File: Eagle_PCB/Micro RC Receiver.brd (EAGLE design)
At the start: 33 x 21.6 mm, 22 parts, among them IC2 TB6612FNG, Q1 CSTCC8M00G53-R0, U1 MIC5205-3.3, U2 ATMEGA328P_TQFP

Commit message: V 1.3
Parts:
- added C3: 10uF, SparkFun-Capacitors:EIA3216
- added R2: 20k, rcl:R0805
- added R3: 10k, rcl:R0805
- moved C6 4.13 mm to (14.3, 15.1), turned to 180 degrees
- moved R1 3.33 mm to (14.3, 13.0)
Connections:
- net A7: now also R2.1, R3.2
- net D3: now also IC2.15; no longer IC2.17
- net D5: now also IC2.17; no longer IC2.15
- net GND: now also C3.C, R3.1
- net VBAT: now also C3.A, R2.2
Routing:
- net A3: track 50.8 -> 23.0 mm
- net RESET: track 26.3 -> 19.2 mm
- net A7: track 0.00 -> 5.68 mm
- net VBAT: track 0.00 -> 4.41 mm
- net A2: track 29.6 -> 25.7 mm
- net VCC: track 38.3 -> 34.5 mm
- net A0: track 51.3 -> 47.6 mm
- net D5: track 22.1 -> 25.4 mm
- net A1: track 26.4 -> 29.4 mm
- net GND: track 58.7 -> 60.3 mm, vias 10 -> 13
- net D3: track 17.9 -> 19.2 mm
- net D9: track 17.3 -> 18.1 mm
- net RXI: track 37.1 -> 36.4 mm
- net TXO: track 34.0 -> 33.4 mm
- net D6: track 21.8 -> 22.3 mm
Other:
- board text added: "Micro RC Receiver V1.3"
- board text removed: "Micro RC Receiver V1.1"

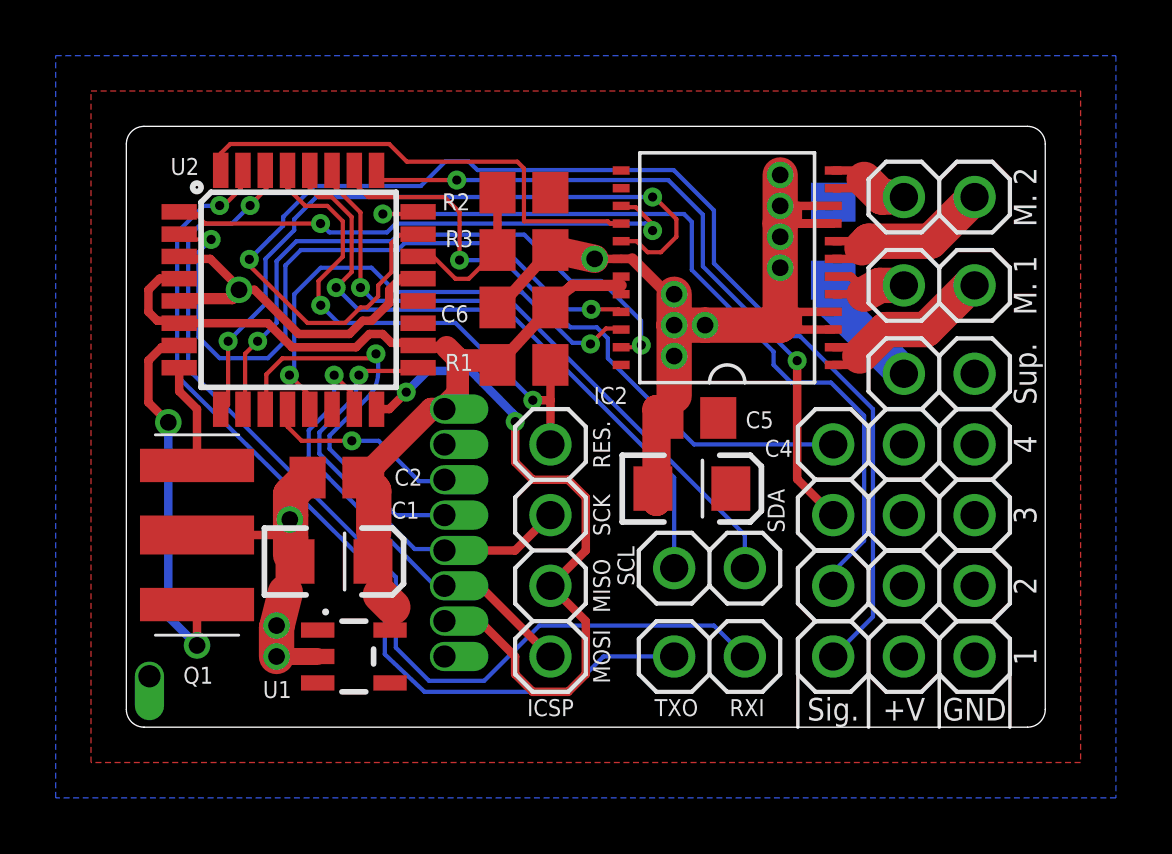
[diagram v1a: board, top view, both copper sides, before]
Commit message: V1.4
GND plane and decoupling improved
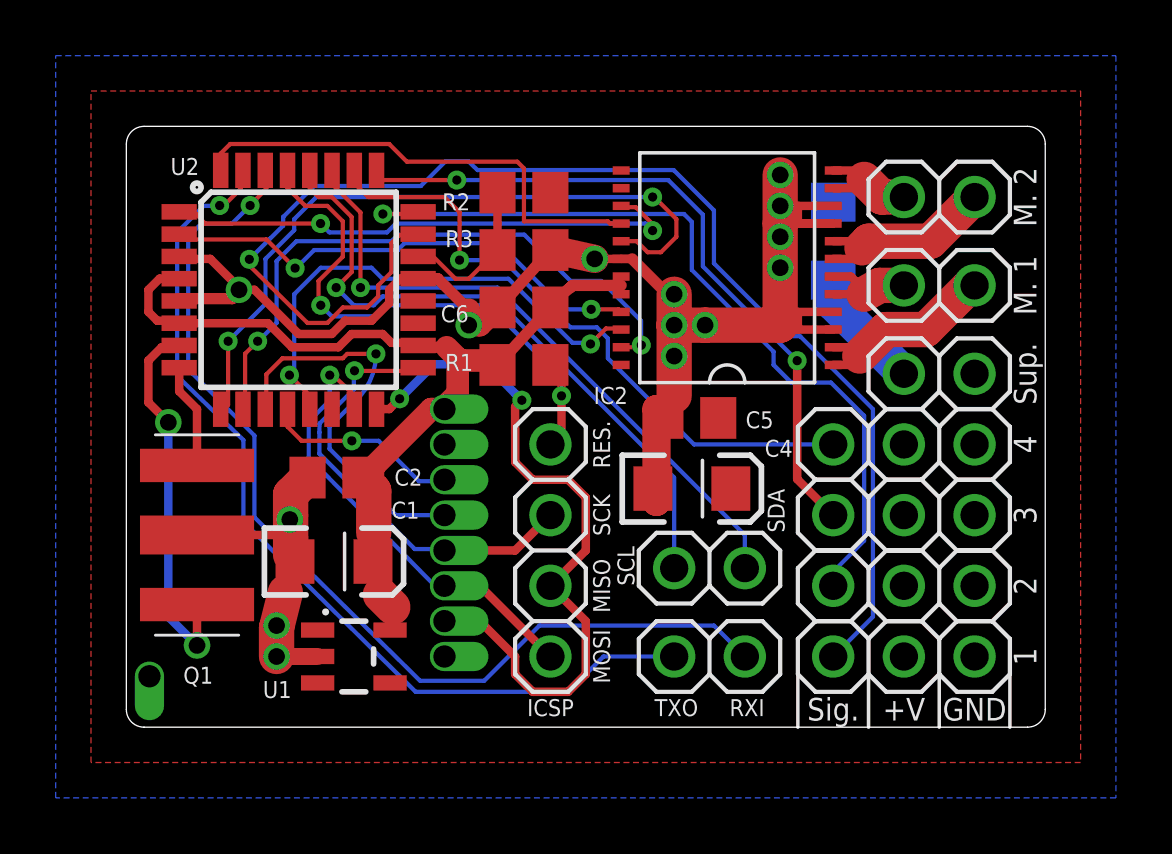
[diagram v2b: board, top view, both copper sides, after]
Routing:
- net D4: track 24.8 -> 17.8 mm
- net GND: track 60.3 -> 64.4 mm, vias 13 -> 14
- net RESET: track 19.2 -> 20.6 mm
- net MISO: track 25.1 -> 26.0 mm
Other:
- board text added: "Micro RC Receiver V1.4"
- board text removed: "Micro RC Receiver V1.3"

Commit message: V1.5: board slightly optimised, Gerbers included
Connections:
- net GND: now also IC1.9
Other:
- board text added: "Micro RC Receiver V1.5"
- board text removed: "Micro RC Receiver V1.4"
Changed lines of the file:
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@@
 <text x="32.7025" y="12.7" size="0.8128" layer="25" rot="R90" align="bottom-center">Sup.</text>
 <text x="15.24" y="0.396875" size="0.6096" layer="25" align="bottom-center">ICSP</text>
-<text x="20.32" y="1.27" size="0.8128" layer="22" rot="MR180" align="center">Micro RC Receiver V1.4</text>
+<text x="20.32" y="1.27" size="0.8128" layer="22" rot="MR180" align="center">Micro RC Receiver V1.5</text>
 <text x="18.25625" y="5.794375" size="0.6096" layer="25" rot="R90" align="bottom-center">SCL</text>
 <text x="23.65375" y="7.77875" size="0.6096" layer="25" rot="R90" align="bottom-center">SDA</text>
@@
 <via x="4.048125" y="15.71625" extent="1-16" drill="0.6"/>
 <via x="12.303125" y="14.44625" extent="1-16" drill="0.6"/>
+<contactref element="IC1" pad="9"/>
 </signal>
 <signal name="VCC">
